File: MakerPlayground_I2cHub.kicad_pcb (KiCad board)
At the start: 2 copper layers, 37 x 20 mm, 14 parts, among them J1 Conn_01x04, J2 Conn_01x04, J3 Conn_01x04, J4 Conn_01x04, J5 Conn_01x04

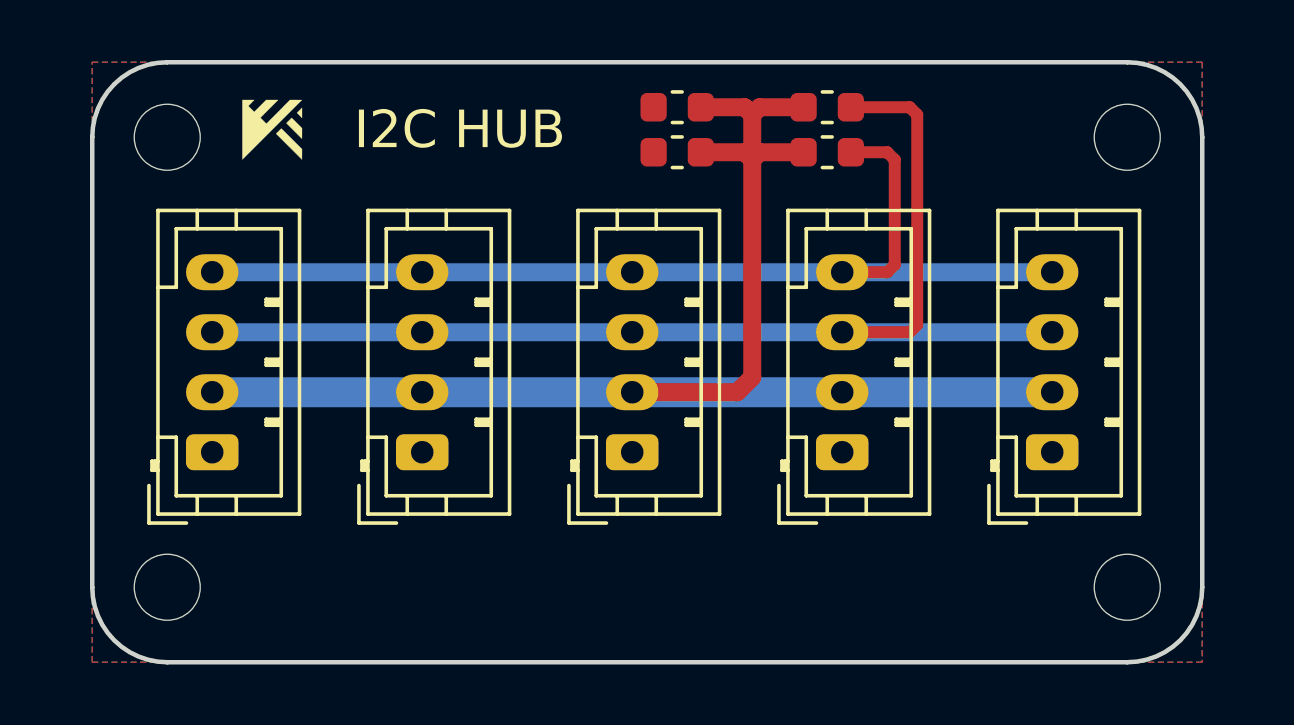
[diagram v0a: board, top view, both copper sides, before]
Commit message: Add more capacitors & new capacitors, resistors alignment.
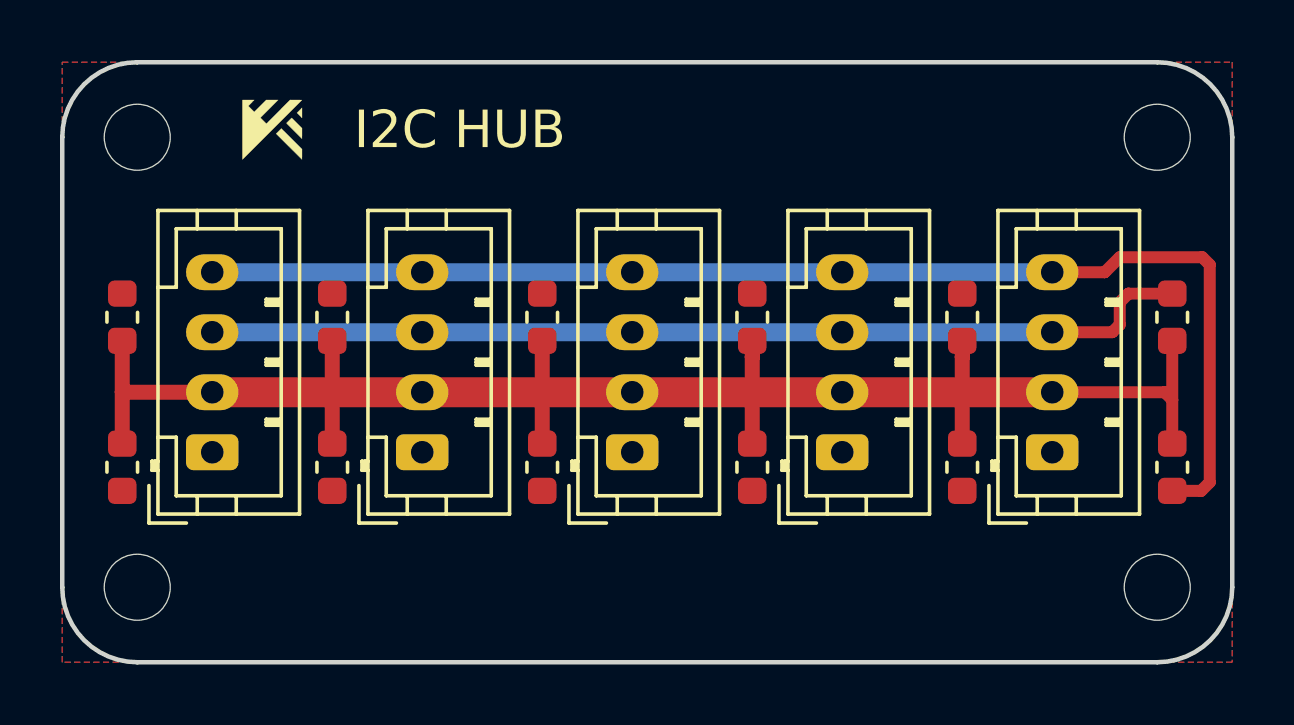
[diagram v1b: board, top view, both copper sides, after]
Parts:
- added C10: 1uF, Capacitor_SMD:C_0603_1608Metric, F.Cu at (119.5, 92.5)
- added C3: 0.1uF, Capacitor_SMD:C_0603_1608Metric, F.Cu at (133.5, 87.5)
- added C4: 0.1uF, Capacitor_SMD:C_0603_1608Metric, F.Cu at (140.5, 87.5)
- added C5: 0.1uF, Capacitor_SMD:C_0603_1608Metric, F.Cu at (147.5, 87.5)
- added C6: 0.1uF, Capacitor_SMD:C_0603_1608Metric, F.Cu at (119.5, 87.5)
- added C7: 1uF, Capacitor_SMD:C_0603_1608Metric, F.Cu at (133.5, 92.5)
- added C8: 1uF, Capacitor_SMD:C_0603_1608Metric, F.Cu at (140.5, 92.5)
- added C9: 1uF, Capacitor_SMD:C_0603_1608Metric, F.Cu at (147.5, 92.5)
- moved C2 16.6 mm to (126.5, 92.5), turned to 270 degrees
- moved R1 15.6 mm to (154.5, 92.5), turned to 270 degrees
- moved R2 13.5 mm to (154.5, 87.5), turned to 90 degrees
- moved C1 12.7 mm to (126.5, 87.5), turned to 90 degrees
- moved REF** 1.00 mm to (154.0, 81.5)
- moved REF** 1.00 mm to (154.0, 96.5)
- moved REF** 1.00 mm to (120.0, 96.5)
- moved REF** 1.00 mm to (120.0, 81.5)
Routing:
- net VCC: track 48.2 -> 55.7 mm
- net SCL: track 34.9 -> 42.2 mm
- net SDA: track 39.9 -> 33.0 mm
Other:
- board size 37 x 20 mm -> 39 x 20 mm
